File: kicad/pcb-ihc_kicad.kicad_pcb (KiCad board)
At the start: 2 copper layers, 100 x 160 mm, 77 parts, among them J1 D-IN with pullup, J10 D-IN with pulldown, J11 2x N-Mosfet, J2 K1 - PD5, J3 K2 - PB7, J4 K3 - PB6, J5 K4 - PD4, J6 K5 - PD3, J7 K6 - PD2, J8 K7 - PD1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

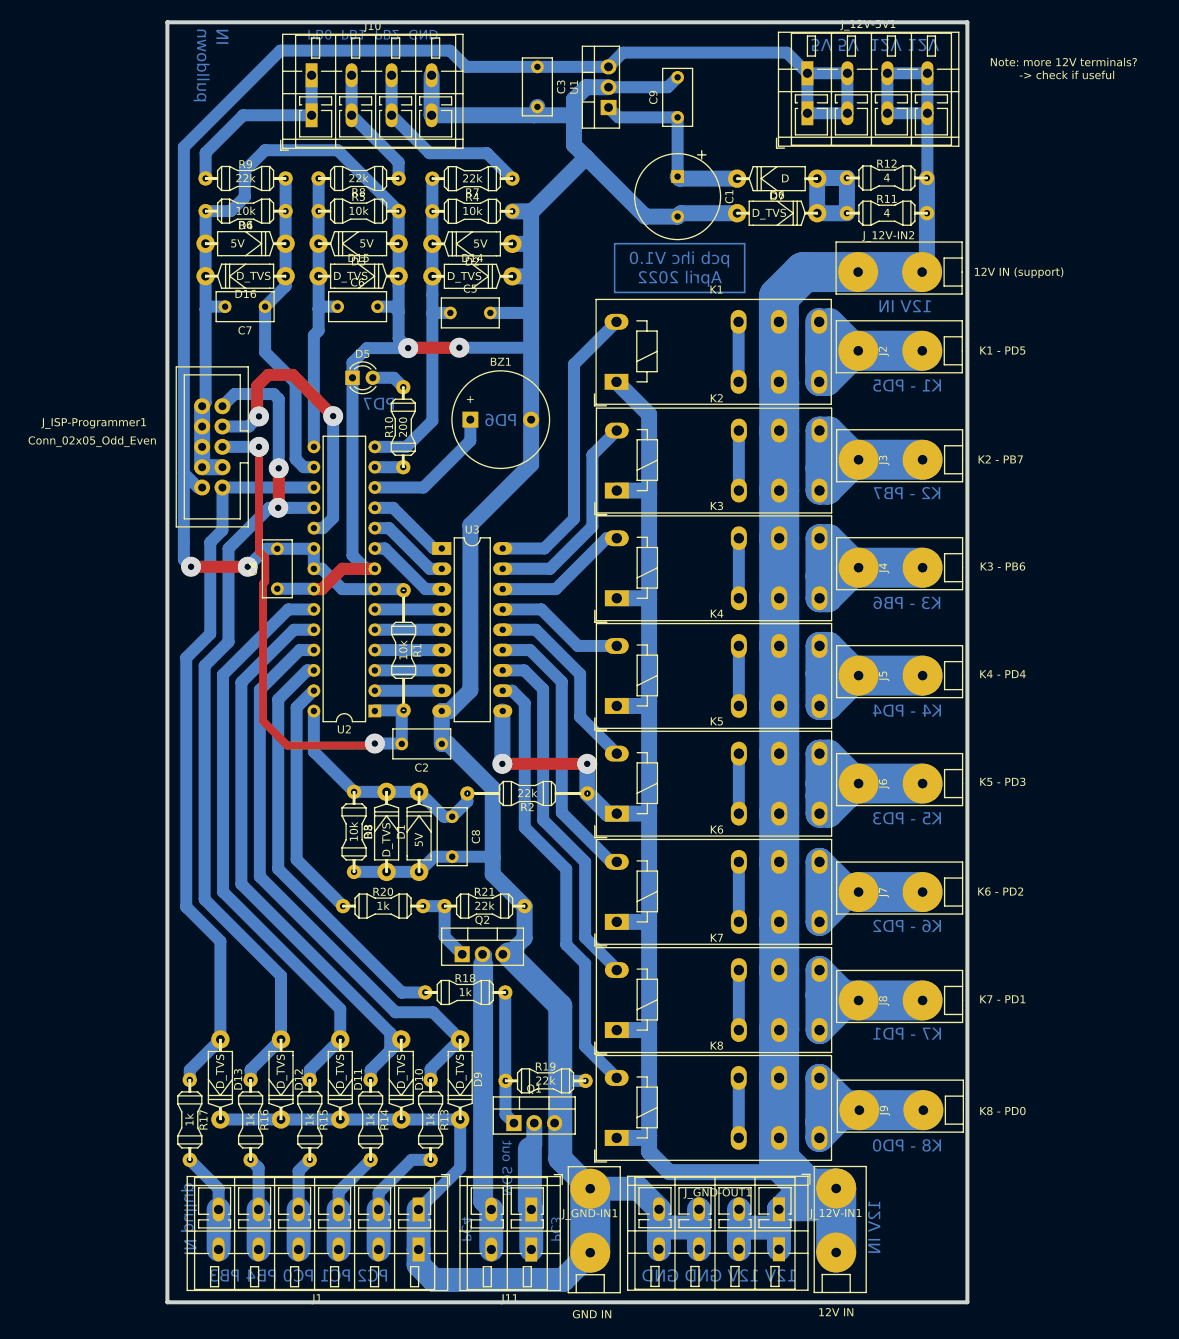
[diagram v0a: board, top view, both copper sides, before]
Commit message: Move text to User1 layer, adjust positions
Move text that should be engraved to pcb from copper-back layer to user1
layer (=> can be handled / processed separately with other parameters by
pcb2gcode)
also make line width to 0.3 for previous smaller text
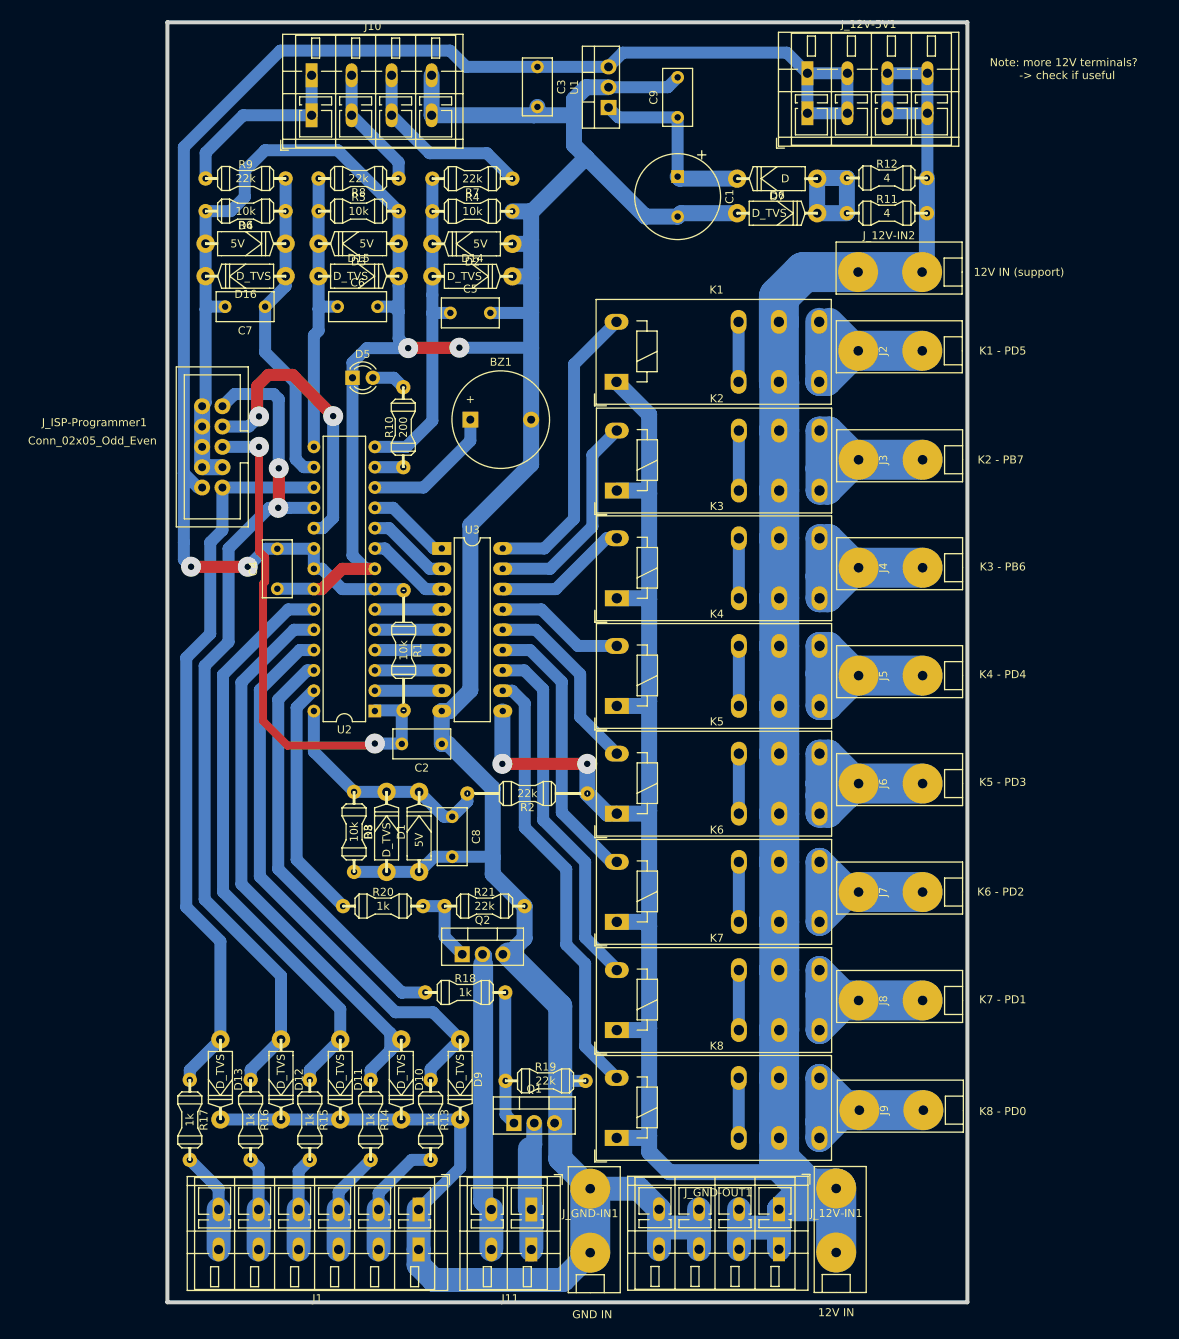
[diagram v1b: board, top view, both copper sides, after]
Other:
- board text added: "ISP"
- board text removed: "TEST text PC1"
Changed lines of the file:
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@@
     (pad_to_mask_clearance 0)
     (pcbplotparams
-      (layerselection 0x0001000_ffffffff)
+      (layerselection 0x0041000_ffffffff)
       (disableapertmacros false)
       (usegerberextensions false)
@@
       (net 10 "Net-(J8-Pad1)") (pinfunction "Pin_1") (pintype "passive"))
   )
-  (gr_rect (start 120.904 42.672) (end 137.16 48.768) (layer "B.Cu") (width 0.2) (fill none))
   (gr_rect (start 165 15) (end 65 175) (layer "Edge.Cuts") (width 0.5) (fill none))
-  (gr_text "IN \npulldown" (at 70.612 15.748 270) (layer "B.Cu")
+  (gr_rect (start 120.904 42.672) (end 137.16 48.768) (layer "User.1") (width 0.3) (fill none))
+  (gr_text "Note: more 12V terminals?\n  -> check if useful" (at 177.038 20.828) (layer "F.SilkS")
+    (effects (font (size 1 1) (thickness 0.15)))
+  )
+  (gr_text "IN \npulldown" (at 70.612 15.748 270) (layer "User.1")
     (effects (font (size 1.5 1.5) (thickness 0.3)) (justify right mirror))
   )
-  (gr_text "PC4" (at 102.362 165.862 270) (layer "B.Cu")
-    (effects (font (size 1.2 1.2) (thickness 0.2)) (justify mirror))
+  (gr_text "PC4" (at 102.362 165.862 270) (layer "User.1")
+    (effects (font (size 1.2 1.2) (thickness 0.3)) (justify mirror))
   )
-  (gr_text "PC2 PC1 PC0 PB4 PB3" (at 81.407 171.704) (layer "B.Cu")
+  (gr_text "PC2 PC1 PC0 PB4 PB3" (at 81.407 171.958) (layer "User.1")
     (effects (font (size 1.5 1.5) (thickness 0.3)) (justify mirror))
   )
-  (gr_text "K1 - PD5" (at 157.48 60.452) (layer "B.Cu")
+  (gr_text "K1 - PD5" (at 157.48 60.96) (layer "User.1")
     (effects (font (size 1.5 1.5) (thickness 0.3)) (justify mirror))
   )
-  (gr_text "PD6" (at 106.68 64.77) (layer "B.Cu")
+  (gr_text "PD6" (at 106.172 61.468) (layer "User.1")
     (effects (font (size 1.5 1.5) (thickness 0.3)) (justify mirror))
   )
-  (gr_text "K8 - PD0" (at 157.48 155.448) (layer "B.Cu")
+  (gr_text "K8 - PD0" (at 157.48 156.21) (layer "User.1")
     (effects (font (size 1.5 1.5) (thickness 0.3)) (justify mirror))
   )
-  (gr_text "PD7" (at 91.44 62.738) (layer "B.Cu")
+  (gr_text "PD7" (at 91.948 63.246) (layer "User.1")
     (effects (font (size 1.5 1.5) (thickness 0.3)) (justify mirror))
   )
-  (gr_text "K3 - PB6" (at 157.48 87.63) (layer "B.Cu")
+  (gr_text "K3 - PB6" (at 157.48 88.138) (layer "User.1")
     (effects (font (size 1.5 1.5) (thickness 0.3)) (justify mirror))
   )
-  (gr_text "PB0  PB1  PB2  GND" (at 90.678 16.51 180) (layer "B.Cu")
-    (effects (font (size 1.2 1.2) (thickness 0.2)) (justify mirror))
+  (gr_text "PB0  PB1  PB2  GND" (at 90.678 16.51 180) (layer "User.1")
+    (effects (font (size 1.2 1.2) (thickness 0.3)) (justify mirror))
   )
-  (gr_text "IN pullup" (at 67.818 164.592 270) (layer "B.Cu")
+  (gr_text "IN pullup" (at 67.564 164.846 270) (layer "User.1")
     (effects (font (size 1.5 1.5) (thickness 0.3)) (justify mirror))
   )
-  (gr_text "pcb ihc V1.0\nApril 2022" (at 129.032 45.72) (layer "B.Cu")
+  (gr_text "pcb ihc V1.0\nApril 2022" (at 129.032 45.72) (layer "User.1")
     (effects (font (size 1.5 1.5) (thickness 0.3)) (justify mirror))
   )
-  (gr_text "K5 - PD3" (at 157.48 114.554) (layer "B.Cu")
+  (gr_text "K5 - PD3" (at 157.48 115.062) (layer "User.1")
     (effects (font (size 1.5 1.5) (thickness 0.3)) (justify mirror))
   )
-  (gr_text "5V 5V  12V 12V" (at 153.416 17.78 180) (layer "B.Cu")
+  (gr_text "5V 5V  12V 12V" (at 153.416 17.526 180) (layer "User.1")
     (effects (font (size 1.5 1.5) (thickness 0.3)) (justify mirror))
   )
-  (gr_text "12V 12V GND GND" (at 133.985 171.704) (layer "B.Cu")
+  (gr_text "12V 12V GND GND" (at 133.985 171.958) (layer "User.1")
     (effects (font (size 1.5 1.5) (thickness 0.3)) (justify mirror))
   )
-  (gr_text "12V IN" (at 153.416 165.608 90) (layer "B.Cu")
+  (gr_text "12V IN" (at 153.416 165.608 90) (layer "User.1")
     (effects (font (size 1.5 1.5) (thickness 0.3)) (justify mirror))
   )
-  (gr_text "MOS out" (at 107.442 158.242 270) (layer "B.Cu")
-    (effects (font (size 1.2 1.2) (thickness 0.2)) (justify mirror))
+  (gr_text "MOS out" (at 107.442 158.242 270) (layer "User.1")
+    (effects (font (size 1.2 1.2) (thickness 0.3)) (justify mirror))
   )
-  (gr_text "PC3" (at 113.538 165.862 270) (layer "B.Cu")
-    (effects (font (size 1.2 1.2) (thickness 0.2)) (justify mirror))
+  (gr_text "PC3" (at 113.538 165.862 270) (layer "User.1")
+    (effects (font (size 1.2 1.2) (thickness 0.3)) (justify mirror))
   )
-  (gr_text "12V IN" (at 157.226 50.546) (layer "B.Cu")
+  (gr_text "12V IN" (at 157.226 50.8) (layer "User.1")
     (effects (font (size 1.5 1.5) (thickness 0.3)) (justify mirror))
   )
-  (gr_text "K7 - PD1" (at 157.48 141.478) (layer "B.Cu")
+  (gr_text "ISP" (at 73.66 58.166) (layer "User.1")
     (effects (font (size 1.5 1.5) (thickness 0.3)) (justify mirror))
   )
-  (gr_text "K4 - PD4" (at 157.48 101.092) (layer "B.Cu")
+  (gr_text "K7 - PD1" (at 157.48 142.24) (layer "User.1")
     (effects (font (size 1.5 1.5) (thickness 0.3)) (justify mirror))
   )
-  (gr_text "K2 - PB7" (at 157.48 73.914) (layer "B.Cu")
+  (gr_text "K4 - PD4" (at 157.48 101.6) (layer "User.1")
     (effects (font (size 1.5 1.5) (thickness 0.3)) (justify mirror))
   )
-  (gr_text "K6 - PD2" (at 157.48 128.016) (layer "B.Cu")
+  (gr_text "K2 - PB7" (at 157.48 74.676) (layer "User.1")
     (effects (font (size 1.5 1.5) (thickness 0.3)) (justify mirror))
   )
-  (gr_text "Note: more 12V terminals?\n  -> check if useful" (at 177.038 20.828) (layer "F.SilkS")
-    (effects (font (size 1 1) (thickness 0.15)))
-  )
-  (gr_text "TEST text PC1" (at 158.75 170.942) (layer "User.1")
-    (effects (font (size 1 1) (thickness 0.15)))
+  (gr_text "K6 - PD2" (at 157.48 128.778) (layer "User.1")
+    (effects (font (size 1.5 1.5) (thickness 0.3)) (justify mirror))
   )
   (segment (start 84.328 85.852) (end 86.868 83.312) (width 1.5) (layer "F.Cu") (net 1))

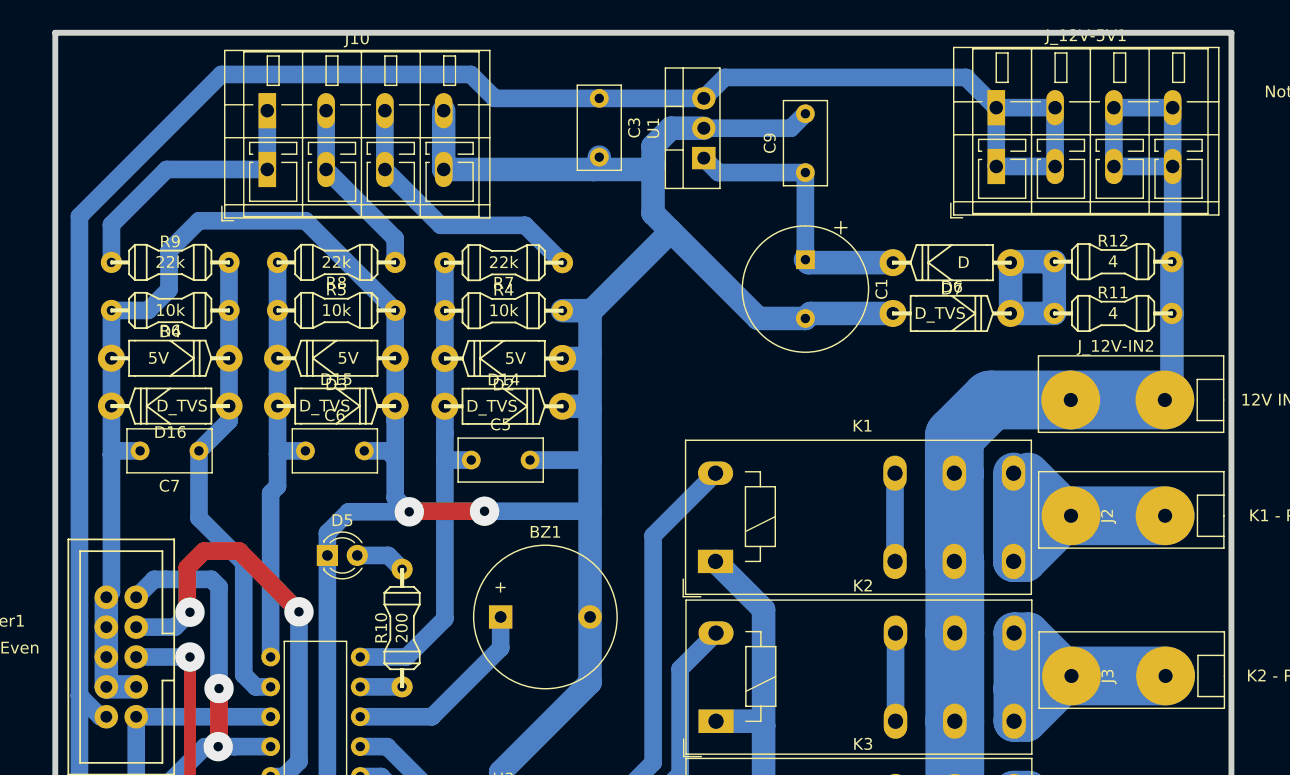
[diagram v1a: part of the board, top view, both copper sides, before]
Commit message: Reduce length of pcb
Layout: move top components closer together to have more "free space" on
the top thus more tolerance when milling
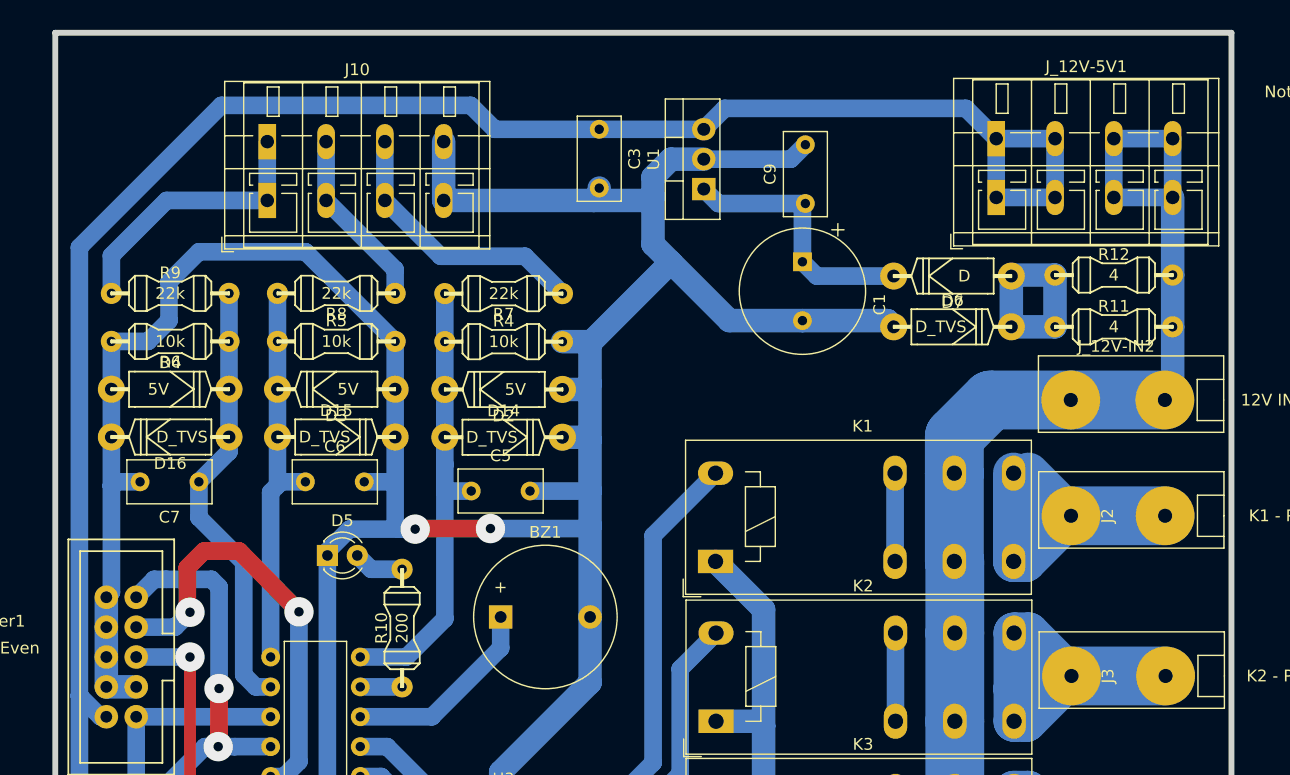
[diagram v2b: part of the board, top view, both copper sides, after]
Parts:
- moved D15 2.63 mm to (88.9, 49.4)
- moved D16 2.63 mm to (74.8, 49.4)
- moved D3 2.63 mm to (88.9, 45.3)
- moved D4 2.63 mm to (74.8, 45.3)
- moved R5 2.63 mm to (88.9, 41.2)
- moved R6 2.63 mm to (74.8, 41.2)
- moved R7 2.63 mm to (103.1, 37.2)
- moved J10 2.63 mm to (83.0, 24.3)
- moved J_12V-5V1 2.63 mm to (145.0, 24.0)
- moved U1 2.63 mm to (120.1, 28.3)
- moved C3 2.63 mm to (111.2, 23.2)
- moved C5 2.63 mm to (100.4, 54.0)
- moved C6 2.63 mm to (86.3, 53.2)
- moved C7 2.63 mm to (77.2, 53.2)
- moved C9 2.63 mm to (128.8, 29.5)
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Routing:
- net GND: track 510.0 -> 500.0 mm
- net /IN pulldown 2: track 36.3 -> 33.7 mm
- net +12V: track 383.8 -> 381.2 mm
- net +5V: track 192.6 -> 190.0 mm
- net /IN pulldown 1: track 41.1 -> 38.4 mm
- net /IN pulldown 3: track 40.4 -> 37.8 mm
- net Net-(C1-Pad1): track 24.1 -> 22.5 mm

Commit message: Minor optimization of text position
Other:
- board text added: "pcb ihc V1.1 April 2022"
- board text removed: "pcb ihc V1.0 April 2022"
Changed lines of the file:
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@@
     (effects (font (size 1.5 1.5) (thickness 0.3)) (justify right mirror))
   )
-  (gr_text "PC4" (at 102.362 165.862 270) (layer "User.1")
+  (gr_text "PC4" (at 102.2604 165.862 270) (layer "User.1")
     (effects (font (size 1.2 1.2) (thickness 0.3)) (justify mirror))
   )
-  (gr_text "PC2 PC1 PC0 PB4 PB3" (at 81.407 171.958) (layer "User.1")
+  (gr_text "PC2 PC1 PC0 PB4 PB3" (at 81.1784 171.958) (layer "User.1")
     (effects (font (size 1.5 1.5) (thickness 0.3)) (justify mirror))
   )
@@
     (effects (font (size 1.5 1.5) (thickness 0.3)) (justify mirror))
   )
-  (gr_text "PB0  PB1  PB2  GND" (at 90.674 18.796 180) (layer "User.1")
+  (gr_text "PB0  PB1  PB2  GND" (at 90.6272 18.4912 180) (layer "User.1")
     (effects (font (size 1.2 1.2) (thickness 0.3)) (justify mirror))
   )
@@
     (effects (font (size 1.5 1.5) (thickness 0.3)) (justify mirror))
   )
-  (gr_text "pcb ihc V1.0\nApril 2022" (at 122.936 45.974) (layer "User.1")
+  (gr_text "pcb ihc V1.1\nApril 2022" (at 122.936 45.974) (layer "User.1")
     (effects (font (size 1.5 1.5) (thickness 0.3)) (justify mirror))
   )
@@
     (effects (font (size 1.5 1.5) (thickness 0.3)) (justify mirror))
   )
-  (gr_text "MOS out" (at 107.442 158.242 270) (layer "User.1")
+  (gr_text "MOS out" (at 107.2134 158.115 270) (layer "User.1")
     (effects (font (size 1.2 1.2) (thickness 0.3)) (justify mirror))
   )
-  (gr_text "PC3" (at 113.538 165.862 270) (layer "User.1")
+  (gr_text "PC3" (at 113.5888 165.862 270) (layer "User.1")
     (effects (font (size 1.2 1.2) (thickness 0.3)) (justify mirror))
   )
@@
     (effects (font (size 1.5 1.5) (thickness 0.3)) (justify mirror))
   )
-  (gr_text "ISP" (at 73.152 58.166) (layer "User.1")
+  (gr_text "ISP" (at 73.4568 58.1152) (layer "User.1")
     (effects (font (size 1.5 1.5) (thickness 0.3)) (justify mirror))
   )

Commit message: Fix incorrect label/text 'PB2' <> 'PB0'
The description of input terminal "in pulldown" was inverted
Fix order on User1 layer and F.Fab in pcbnew
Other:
- board text added: "PB2 PB1 PB0 GND"
- board text removed: "PB0 PB1 PB2 GND"
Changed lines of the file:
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@@
       (effects (font (size 1 1) (thickness 0.15)))
     )
-    (fp_text user "[(1-4): PB0, PB1, PB2, GND]" (at 7.904 -7.652 unlocked) (layer "F.Fab")
+    (fp_text user "[(1-4): PB2, PB1, PB0, GND]" (at 7.904 -7.652 unlocked) (layer "F.Fab")
       (effects (font (size 1 1) (thickness 0.15)))
     )
@@
     (effects (font (size 1.5 1.5) (thickness 0.3)) (justify mirror))
   )
-  (gr_text "PB0  PB1  PB2  GND" (at 90.6272 18.4912 180) (layer "User.1")
+  (gr_text "PB2  PB1  PB0  GND" (at 90.6272 18.4912 180) (layer "User.1")
     (effects (font (size 1.2 1.2) (thickness 0.3)) (justify mirror))
   )
